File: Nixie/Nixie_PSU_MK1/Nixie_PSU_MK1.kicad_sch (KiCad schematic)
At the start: 26 parts, among them Q1 IRF740, Q2 PN2907ABU, U1 MC34063AP

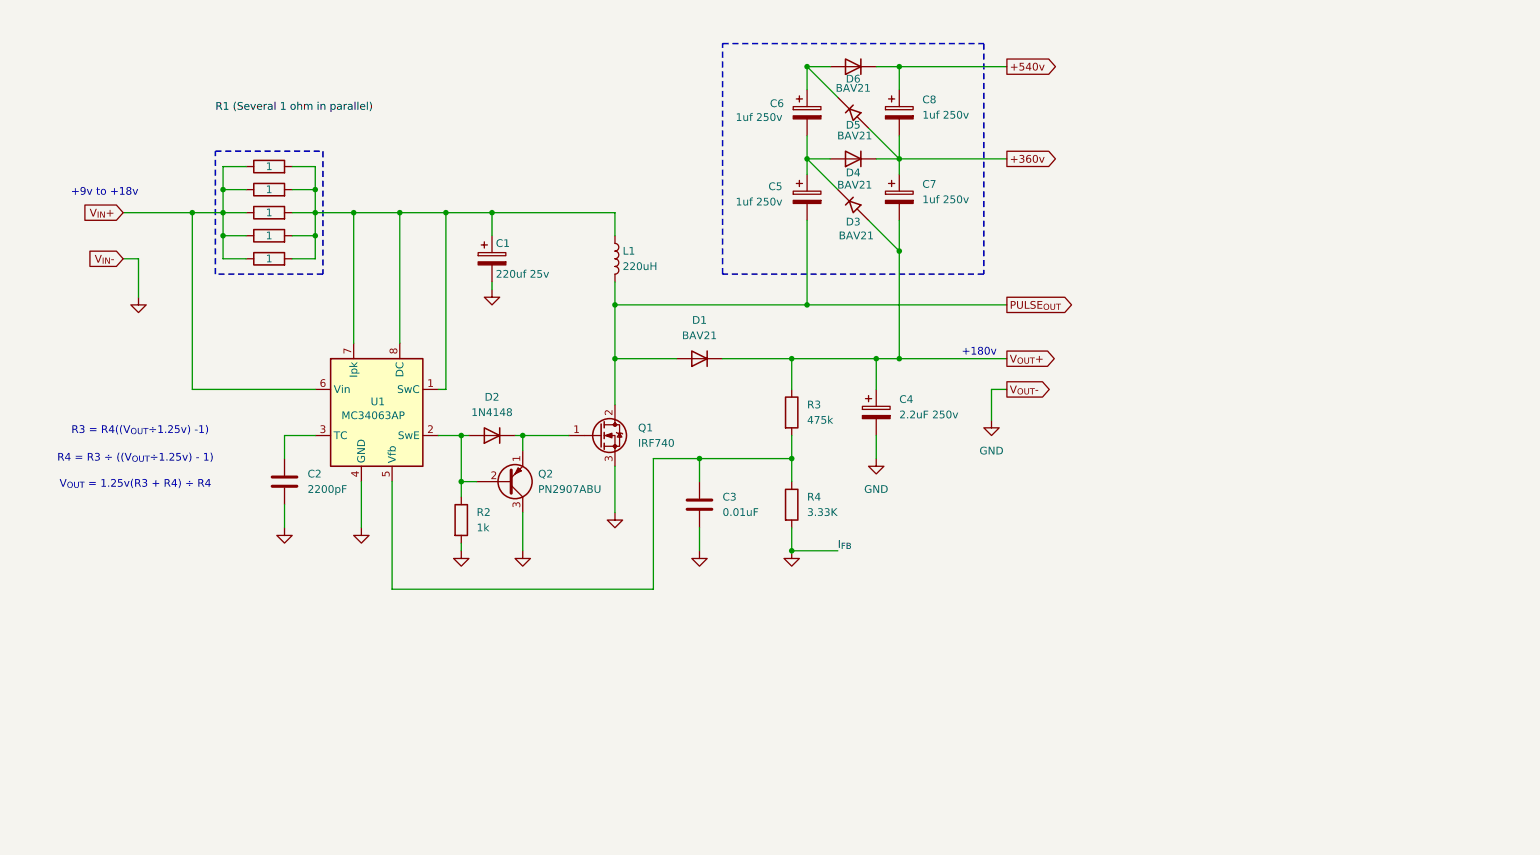
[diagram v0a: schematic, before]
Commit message: Update Nixie PSU
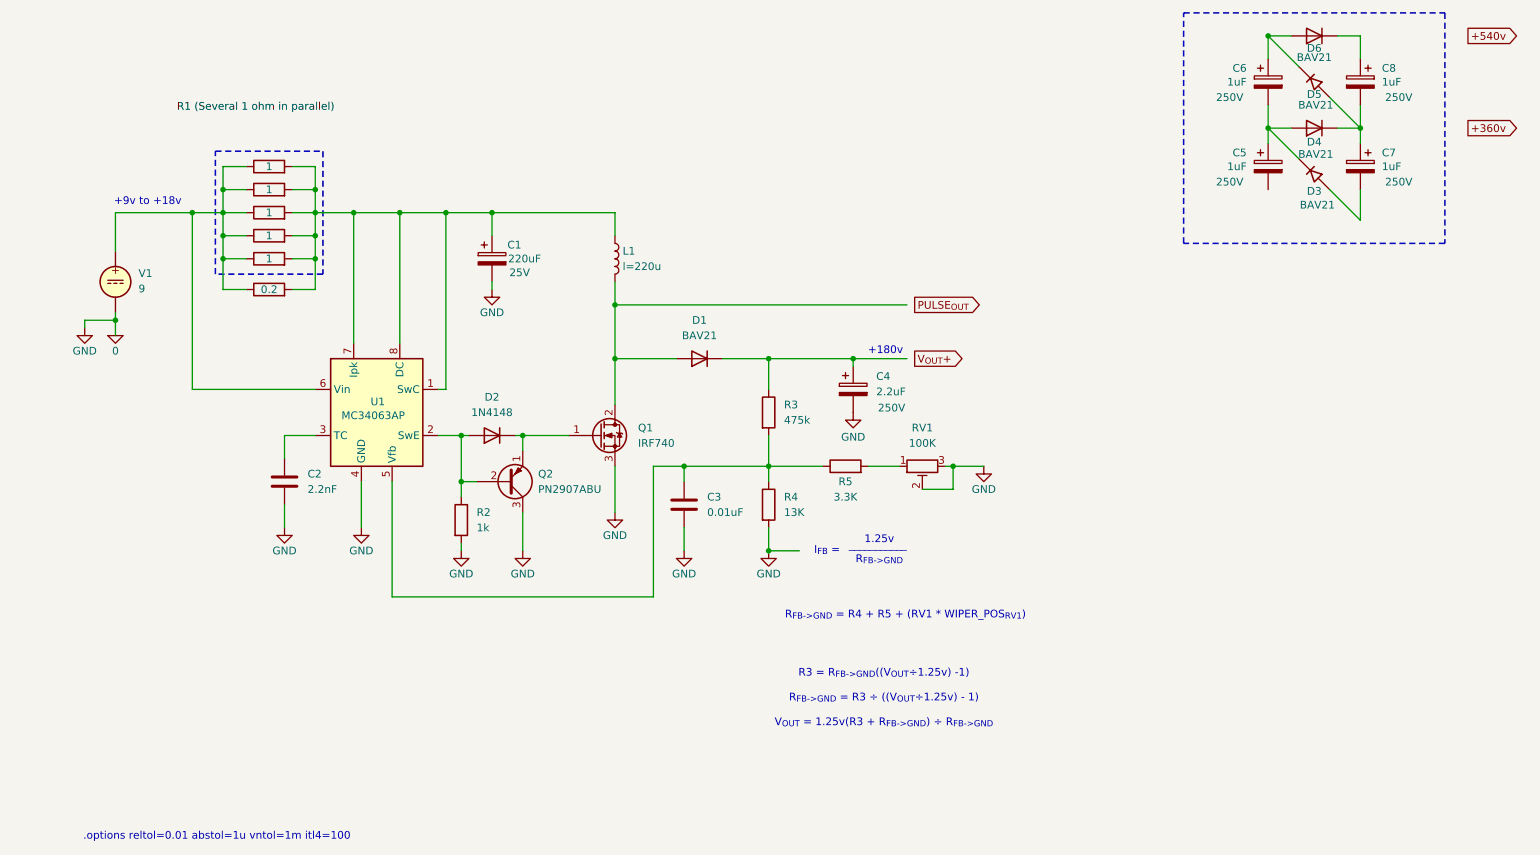
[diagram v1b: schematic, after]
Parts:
- added R1e2: 0.2, Resistor_THT:R_Axial_DIN0207_L6.3mm_D2.5mm_P7.62mm_Horizontal, symbol Device:R
- added R5: 3.3K, symbol Device:R
- added RV1: 100K, Potentiometer_THT:Potentiometer_Bourns_3296W_Vertical, symbol Device:R_Potentiometer_Trim
- added V1: 9, symbol Simulation_SPICE:VDC
- C1: value 220uf 25v -> 220uF; Voltage (none) -> 25V
- C2: value 2200pF -> 2.2nF
- C4: value 2.2uF 250v -> 2.2uF; Voltage (none) -> 250V
- C5, C6, C7, C8: value 1uf 250v -> 1uF; Voltage (none) -> 250V
- L1: value 220uH -> ${SIM.PARAMS}
- R4: value 3.33K -> 13K
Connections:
- net +360v: no longer C7.1, C8.2, D4.1 (K), D5.2 (A)
- net +540v: no longer C8.1, D6.1 (K)
- net PULSE_{OUT}: no longer C5.2, D1.2 (A), L1.2, Q1.2 (D)
- net V_{OUT}+: no longer C4.1, C7.2, D1.1 (K), D3.2 (A), R3.1
- net at C1.1, L1.1, R1a1.2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: now also R1e2.2
- net at C3.1, R3.2, R4.1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: now also R5.1
- net GND renamed 0
- net 0: now also RV1.2, RV1.3, V1.2
- net V_{IN}+: no longer names the net of R1a1.1, R1b1.1, R1c1.1, R1d1.1, R1e1.1, U1.6 (Vin)
- net V_{IN}+: now also R1e2.1, V1.1
- new net: C4.1, D1.1 (K), R3.1
- new net: D1.2 (A), L1.2, Q1.2 (D)
- new net: C8.1, D6.1 (K)
- new net: C7.1, C8.2, D4.1 (K), D5.2 (A)
- new net: C7.2, D3.2 (A)
- new net: R5.2, RV1.1
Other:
- note added: ".options reltol=0.01 abstol=1u vntol=1m itl4=100"
- note added: "1.25v"
- note added: "I_{FB} ="
- note added: "R3 = R_{FB->GND}((V_{OUT}÷1.25v) -1) R_{FB->GND} = R3 ÷ ((V_{OUT}÷1.25v) - 1) V_{OUT} = 1.25v(R3 + R_{FB->GND}) ÷ R_{FB->GND}"
- note added: "R_{FB->GND}"
- note added: "R_{FB->GND} = R4 + R5 + (RV1 * WIPER_POS_{RV1})"
- note added: "___________"
- note removed: "R3 = R4((V_{OUT}÷1.25v) -1)"
- note removed: "R4 = R3 ÷ ((V_{OUT}÷1.25v) - 1)"
- note removed: "V_{OUT} = 1.25v(R3 + R4) ÷ R4"
- moved on the sheet: C3, C4, C6, D3, D4, D5, D6, R3, R4
